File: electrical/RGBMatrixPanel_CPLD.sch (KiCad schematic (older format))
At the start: 40 parts, among them J1 BARREL_JACK, J2 CONN_01X01, J3 CONN_01X01, J4 CONN_01X01, J5 CONN_01X01, J6 CONN_01X06, J7 CONN_02X08, J8 CONN_01X06, J9 CONN_01X03, Q1 Photo_Trans, Q2 CSD17307Q5A, Q3 CSD18531Q5A, U1 PHOTON, U2 LC4032V-44TQFP, U3 LM3150, X1 MTHOLE, X2 MTHOLE, X3 MTHOLE

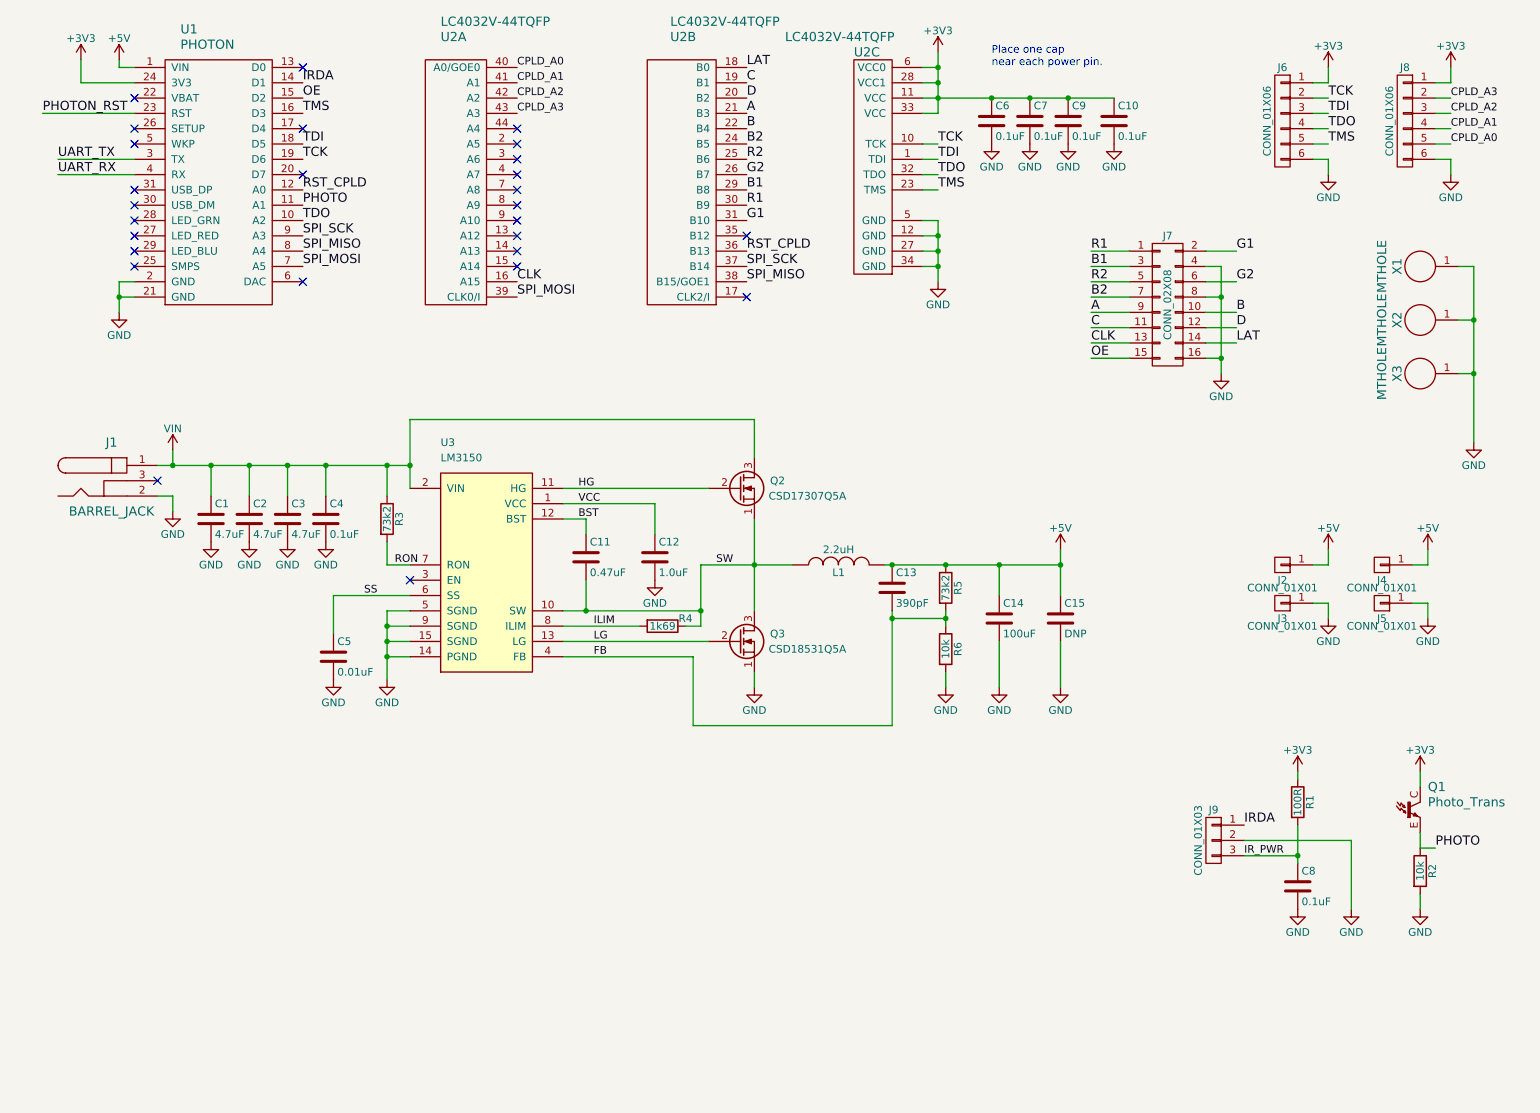
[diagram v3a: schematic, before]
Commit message: Added buck converter
Added an on-board 24V to 5V buck converter to lower the current going
through the connector to a safe level. Now the magic smoke stays safely
contained.
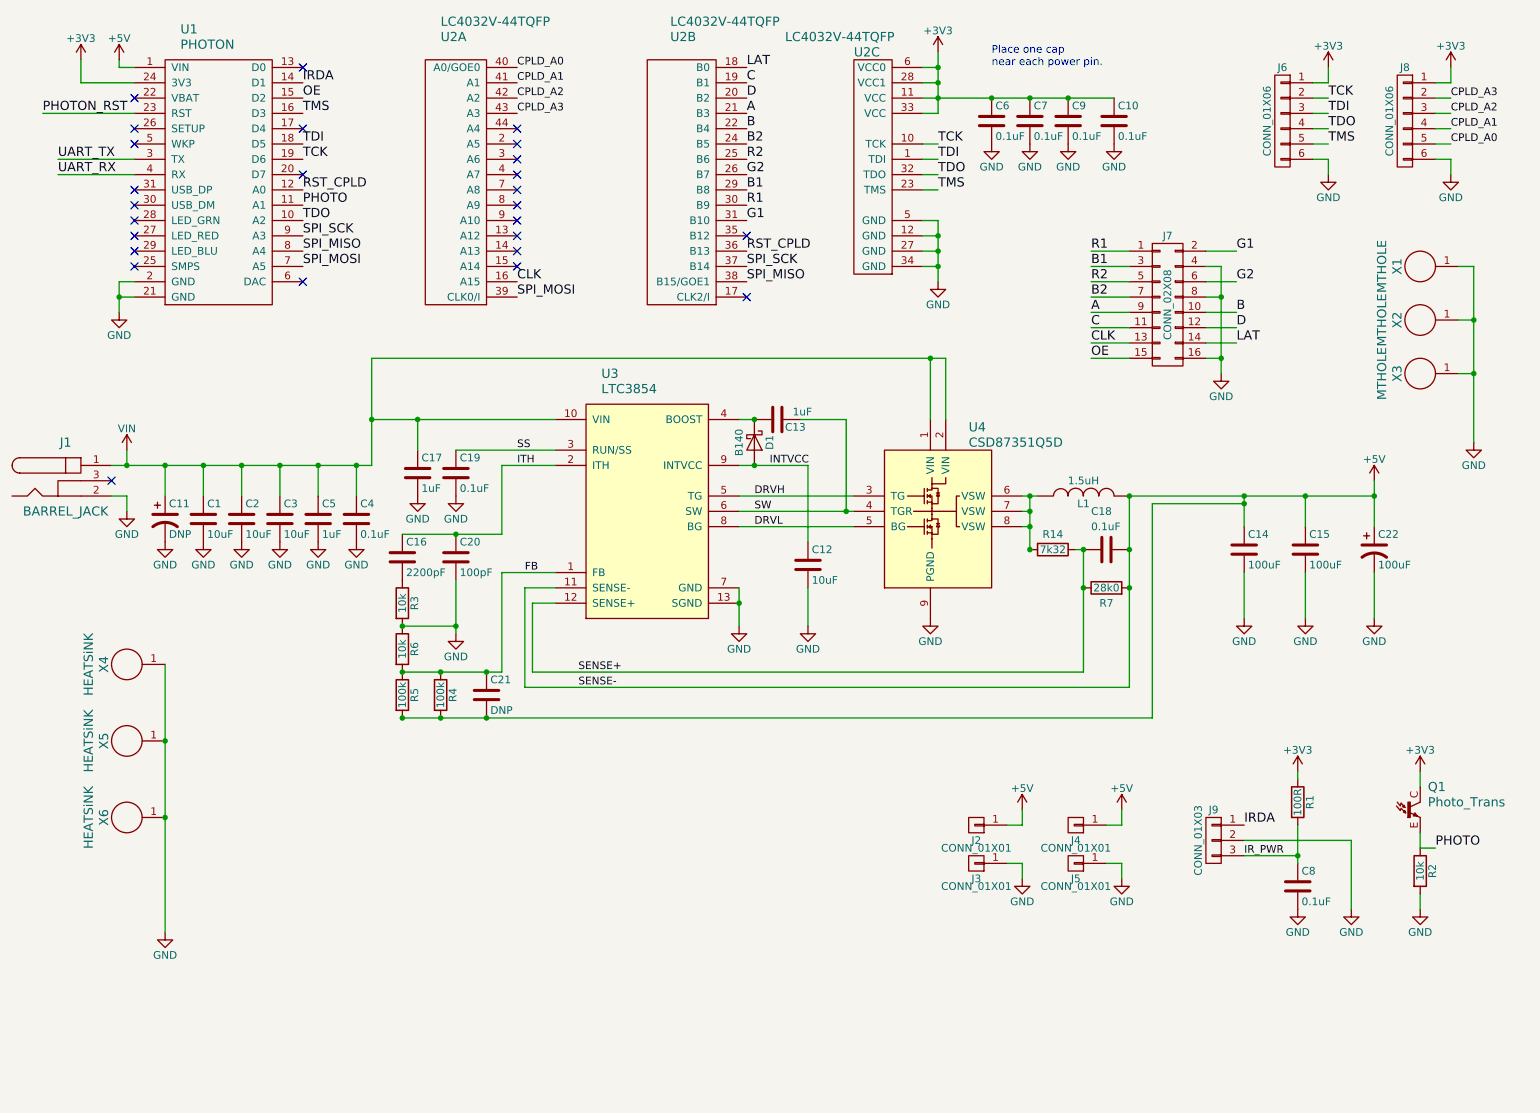
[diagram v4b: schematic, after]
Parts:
- removed C11: 0.47uF, Capacitors_SMD:C_0805, symbol C
- removed Q2: CSD17307Q5A, Reclaimer_Labs:MOSFET_Q5A, symbol Q_NMOS_SGD
- removed Q3: CSD18531Q5A, Reclaimer_Labs:MOSFET_Q5A, symbol Q_NMOS_SGD
- removed U3: LM3150, Reclaimer_Labs:TSSOP-14-0.65mm-EP, symbol LM3150
- added C11: DNP, Capacitors_Tantalum_SMD:CP_Tantalum_Case-D_EIA-7343-31_Reflow, symbol CP1
- added C16: 2200pF, Capacitors_SMD:C_0603, symbol C
- added C17: 1uF, Capacitors_SMD:C_0603, symbol C
- added C18, C19: 0.1uF, Capacitors_SMD:C_0603, symbol C
- added C20: 100pF, Capacitors_SMD:C_0603, symbol C
- added C21: DNP, Capacitors_SMD:C_0603, symbol C
- added C22: 100uF, Capacitors_Tantalum_SMD:CP_Tantalum_Case-D_EIA-7343-31_Reflow, symbol CP1
- added D1: B140, Diodes_SMD:D_SMA_Standard, symbol D_Schottky
- added R14: 7k32, Capacitors_SMD:C_0603, symbol R
- added R7: 28k0, Capacitors_SMD:C_0603, symbol R
- added U3: LTC3854, Reclaimer_Labs:12-MSE, symbol LTC3854
- added U4: CSD87351Q5D, Reclaimer_Labs:CSD87351Q5D, symbol CSD87351Q5D
- added X4, X5, X6: HEATSiNK, Reclaimer_Labs:573100D00010G, symbol MTHOLE
- C1, C2, C3: value 4.7uF -> 10uF; Manufacturer Murata -> Samsung; Manufacturer Part Number GRM31CR71H475KA12L -> CL31A106MBHNNNE
- C10, C9: MacroFab Part Number (none) -> MF-CAP-0603-0.1uF; Manufacturer Yageo -> (none); Manufacturer Part Number CC0603KRX7R9BB103 -> (none); Supplier 1 Digikey -> (none); Supplier 1 Part Number 311-1085-1-ND -> (none)
- C12: value 1.0uF -> 10uF; footprint Capacitors_SMD:C_0603 -> Capacitors_SMD:C_0805; MacroFab Part Number MF-CAP-0603-1uF -> (none); Manufacturer (none) -> Taiyo Yuden; Manufacturer Part Number (none) -> TMK212BBJ106KG-T
- C13: value 390pF -> 1uF; MacroFab Part Number (none) -> MF-CAP-0603-1uF; Manufacturer Samsung -> (none); Manufacturer Part Number CL10B391KC8WPNC -> (none)
- C14: footprint Capacitors_SMD:C_1206 -> Capacitors_SMD:C_1210; Manufacturer Part Number GRM31CR60J107ME39L -> GRM32ER61A107ME20L
- C15: value DNP -> 100uF; footprint Capacitors_SMD:C_1206 -> Capacitors_SMD:C_1210; Manufacturer Part Number GRM31CR60J107ME39L -> GRM32ER61A107ME20L
- C4: footprint Capacitors_SMD:C_0805 -> Capacitors_SMD:C_0603; MacroFab Part Number MF-CAP-0805-0.1uF -> MF-CAP-0603-0.1uF
- C5: value 0.01uF -> 1uF; MacroFab Part Number MF-CAP-0603-0.01uF -> MF-CAP-0603-1uF
- C6, C7, C8: MacroFab Part Number (none) -> MF-CAP-0603-0.1uF; Manufacturer Yageo -> (none); Manufacturer Part Number CC0603KRX7R7BB104 -> (none); Supplier 1 Digikey -> (none); Supplier 1 Part Number 311-1088-1-ND -> (none)
- J6, J8, J9: DNP (none) -> DNP
- L1: value 2.2uH -> 1.5uH; Manufacturer Part Number SRP1270-2R2M -> SRP1270-1R5M
- Q1: footprint Reclaimer_Labs:Photo_Trans_0805 -> Reclaimer_Labs:Photo_Trans_ALS-PT19-315C; Manufacturer Rohm -> Everlight; Manufacturer Part Number RPM-075PTT86 -> ALS-PT19-315C/L177/TR8; Supplier 1 Digikey -> (none); Supplier 1 Part Number 511-1356-1-ND -> (none)
- R1: MacroFab Part Number (none) -> MF-RES-0603-100; Manufacturer Samsung -> (none); Manufacturer Part Number RC1608F101CS -> (none); Supplier 1 Digikey -> (none); Supplier 1 Part Number 1276-3482-1-ND -> (none)
- R2: MacroFab Part Number (none) -> MF-RES-0603-10K; Manufacturer Samsung -> (none); Manufacturer Part Number RC1608F103CS -> (none); Supplier 1 Digikey -> (none); Supplier 1 Part Number 1276-3485-1-ND -> (none)
- R3: value 73k2 -> 10k; MacroFab Part Number (none) -> MF-RES-0603-10K; Manufacturer Yageo -> (none); Manufacturer Part Number RC0603FR-0773K2L -> (none)
- R4: value 1k69 -> 100k; MacroFab Part Number MF-RES-0603-1.69K -> MF-RES-0603-100K
- R5: value 73k2 -> 100k; MacroFab Part Number (none) -> MF-RES-0603-100K; Manufacturer Yageo -> (none); Manufacturer Part Number RC0603FR-0773K2L -> (none)
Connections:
- net ILIM is gone; now on net +5V: R4.2
- net RON is gone; now on net GND: R3.2
- net +5V: now also R5.2, C18.1, C21.2, C22.1, R7.2, U3.11 (SENSE-); no longer C13.1, R5.1
- net FB: now also R4.1, R5.1, R6.2, C21.1, U3.1 (FB); no longer C13.2, R5.2, R6.1
- net GND: now also R6.1, C11.2, C17.2, C19.2, C20.2, C22.2, U3.13 (SGND), U3.7 (GND), U4.9 (PGND), X4.1, X5.1, X6.1; no longer R6.2
- net SS: now also C19.1, U3.3 (RUN/SS); no longer C5.1
- net SW: now also C13.1, U3.6 (SW), U4.4 (TGR); no longer L1.1, R4.1
- net VIN: now also C5.1, C11.1, C17.1, U3.10 (VIN), U4.1 (VIN), U4.2 (VIN); no longer R3.1
- net VCC renamed INTVCC
- net INTVCC: now also D1.2 (A), U3.9 (INTVCC)
- new net: L1.1, R14.2, U4.6 (VSW), U4.7 (VSW), U4.8 (VSW)
- new net: C13.2, D1.1 (K), U3.4 (BOOST)
- new net: C16.2, R3.1
- new net DRVH: U3.5 (TG), U4.3 (TG)
- new net DRVL: U3.8 (BG), U4.5 (BG)
- new net ITH: C16.1, C20.1, U3.2 (ITH)
- new net SENSE+: C18.2, R14.1, R7.1, U3.12 (SENSE+)
- no-connect marks 27 -> 26
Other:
- moved on the sheet: C1, C14, C15, C2, C3, C4, J1, J2, J3, J4, J5, L1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
